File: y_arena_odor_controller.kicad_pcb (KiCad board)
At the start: 2 copper layers, 74.9 x 80.6 mm, 105 parts, among them P1 PWR_JACK_2.1x5.5_SMD_RA, SW1 SPDT_SLIDE_500A_SM, U1 DRV103, U2 DRV103, U3 DRV103, U4 DRV103, U5 DRV103, U6 DRV103, U7 DRV103, U8 DRV103, U9 DRV103

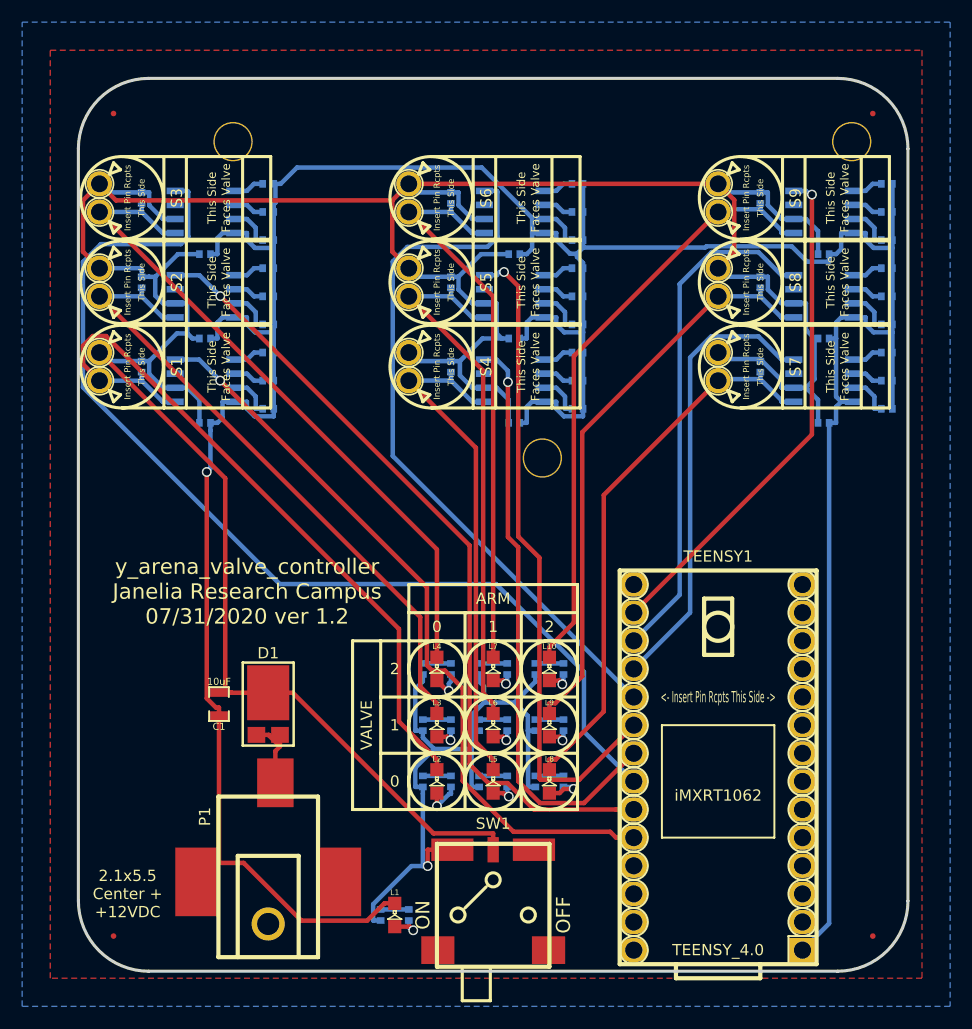
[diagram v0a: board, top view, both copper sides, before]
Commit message: valve -> odor
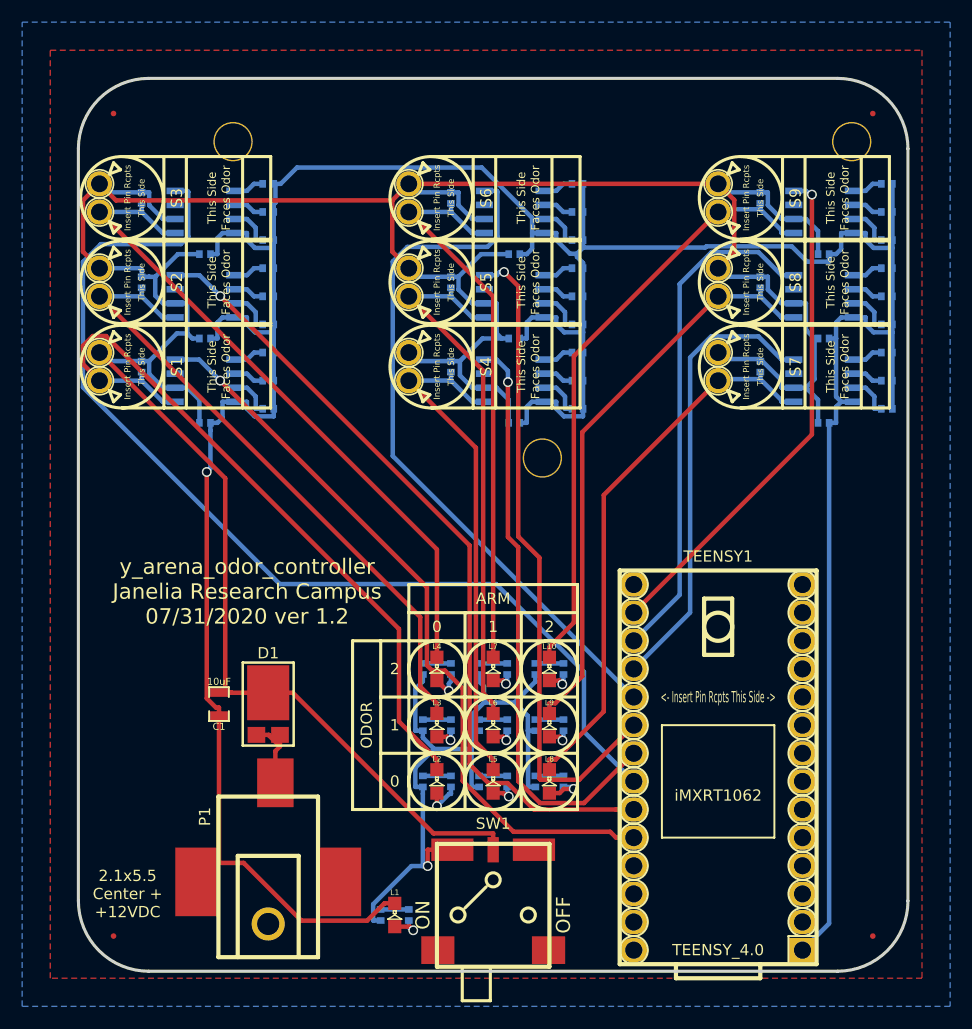
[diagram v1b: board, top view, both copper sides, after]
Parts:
- C1: footprint y_arena_valve_controller:SM0805 -> y_arena_odor_controller:SM0805
- C10, C12, C14, C16, C18, C2, C4, C6, C8, D10, D11, D12, D13, D14, D15, D16, D17, D18, D19, D20, D3, D4, D5, D6, D7, D8, D9: footprint valve_spike_hold:SM0402_POL -> odor_spike_hold:SM0402_POL
- C11, C13, C15, C17, C19, C3, C5, C7, C9, R10, R11, R12, R13, R14, R15, R16, R17, R18, R19, R2, R20, R21, R22, R23, R24, R25, R26, R27, R28, R3, R4, R5, R6, R7, R8, R9: footprint valve_spike_hold:SM0402 -> odor_spike_hold:SM0402
- D1: footprint y_arena_valve_controller:CFP15 -> y_arena_odor_controller:CFP15
- D2: footprint y_arena_valve_controller:SM0402_POL -> y_arena_odor_controller:SM0402_POL
- FID1, FID2, FID3, FID4: footprint y_arena_valve_controller:FIDUCIAL -> y_arena_odor_controller:FIDUCIAL
- L1: footprint y_arena_valve_controller:LED0805 -> y_arena_odor_controller:LED0805
- L10, L2, L3, L4, L5, L6, L7, L8, L9: footprint valve_spike_hold:LED0805 -> odor_spike_hold:LED0805
- MH1, MH2, MH3: footprint y_arena_valve_controller:MOUNTING_HOLE_4-40 -> y_arena_odor_controller:MOUNTING_HOLE_4-40
- P1: footprint y_arena_valve_controller:DCJACK_3PAD_SMD_RA -> y_arena_odor_controller:DCJACK_3PAD_SMD_RA
- R1: footprint y_arena_valve_controller:SM0402 -> y_arena_odor_controller:SM0402
- S1, S2, S3, S4, S5, S6, S7, S8, S9: footprint valve_spike_hold:LEECO_LHDB -> odor_spike_hold:LEECO_LHDB
- SW1: footprint y_arena_valve_controller:SPDT_SLIDE_500A_SM -> y_arena_odor_controller:SPDT_SLIDE_500A_SM
- TEENSY1: footprint y_arena_valve_controller:TEENSY_4.0 -> y_arena_odor_controller:TEENSY_4.0
- U1, U2, U3, U4, U5, U6, U7, U8, U9: footprint valve_spike_hold:SOIC_8 -> odor_spike_hold:SOIC_8
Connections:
- net /ARM_0_VALVE_0 renamed /ARM_0_ODOR_0
- net /ARM_0_VALVE_1 renamed /ARM_0_ODOR_1
- net /ARM_0_VALVE_2 renamed /ARM_0_ODOR_2
- net /ARM_1_VALVE_0 renamed /ARM_1_ODOR_0
- net /ARM_1_VALVE_1 renamed /ARM_1_ODOR_1
- net /ARM_1_VALVE_2 renamed /ARM_1_ODOR_2
- net /ARM_2_VALVE_0 renamed /ARM_2_ODOR_0
- net /ARM_2_VALVE_1 renamed /ARM_2_ODOR_1
- net /ARM_2_VALVE_2 renamed /ARM_2_ODOR_2
- net /valve_0/SH renamed /odor_0/SH
- net /valve_1/SH renamed /odor_1/SH
- net /valve_2/SH renamed /odor_2/SH
- net /valve_3/SH renamed /odor_3/SH
- net /valve_4/SH renamed /odor_4/SH
- net /valve_5/SH renamed /odor_5/SH
- net /valve_6/SH renamed /odor_6/SH
- net /valve_7/SH renamed /odor_7/SH
- net /valve_8/SH renamed /odor_8/SH
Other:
- board text added: "ODOR"
- board text added: "ODOR 0"
- board text added: "ODOR 1"
- board text added: "ODOR 2"
- board text added: "y_arena_odor_controller Janelia Research Campus 07/31/2020 ver 1.2"
- board text removed: "VALVE"
- board text removed: "VALVE 0"
- board text removed: "VALVE 1"
- board text removed: "VALVE 2"
- board text removed: "y_arena_valve_controller Janelia Research Campus 07/31/2020 ver 1.2"

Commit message: Switch arms from columns to rows and use odor instead of valve
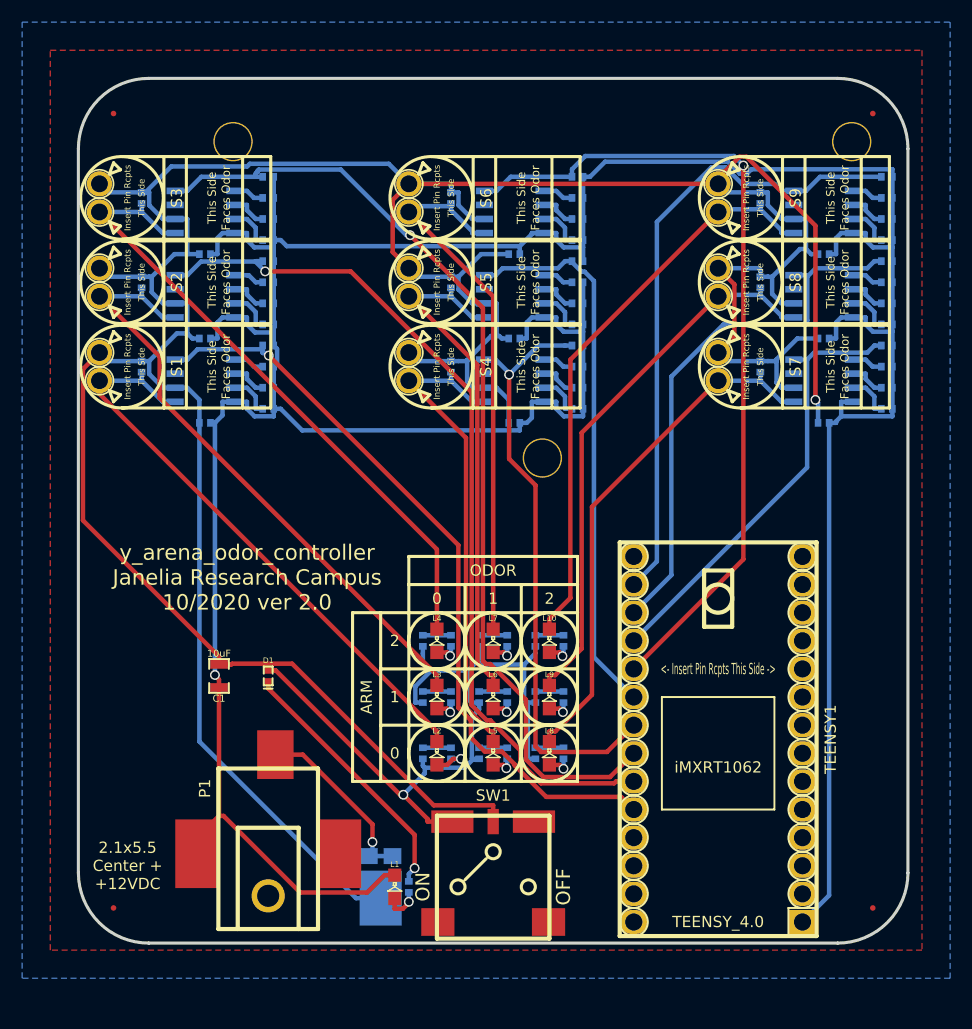
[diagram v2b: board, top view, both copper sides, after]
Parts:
- added R29: 205k, odor_spike_hold:SM0402, B.Cu at (123.8, 80.6)
- added R30: 390, odor_spike_hold:SM0402, B.Cu at (94.6, 106.7)
- added R31: 150k, odor_spike_hold:SM0402, B.Cu at (123.8, 67.3)
- added R32: 150k, odor_spike_hold:SM0402, B.Cu at (123.8, 69.2)
- added R33: 205k, odor_spike_hold:SM0402, B.Cu at (123.8, 73.0)
- added R34: 390, odor_spike_hold:SM0402, B.Cu at (94.6, 101.6)
- added R35: 150k, odor_spike_hold:SM0402, B.Cu at (123.8, 59.7)
- added R36: 150k, odor_spike_hold:SM0402, B.Cu at (123.8, 61.6)
- added R37: 205k, odor_spike_hold:SM0402, B.Cu at (123.8, 65.4)
- D1: value DIODE_SCHOTTKY_45V_10A -> DIODE_LOW_REV_CURRENT_0402; footprint y_arena_odor_controller:CFP15 -> y_arena_odor_controller:SM0402_POL
- D2: value DIODE_LOW_REV_CURRENT_0402 -> DIODE_SCHOTTKY_45V_10A; footprint y_arena_odor_controller:SM0402_POL -> y_arena_odor_controller:CFP15
- MH1, MH2, MH3: value VAL** -> MOUNTING_HOLE_4-40
- R10, R22: value 205k -> 390
- R11, R20, R23, R8: value 390 -> 150k
- R16, R19, R28, R4, R7: value 205k -> 150k
- R17, R5: value 390 -> 205k
- R18, R6: value 150k -> 390
- R21, R9: value 150k -> 205k
- S1, S2, S3, S4, S5, S6, S7, S8, S9: value VAL** -> LEECO_LHDB
- moved R11 58.7 mm to (67.9, 59.7), turned to 270 degrees
- moved R23 49.5 mm to (95.9, 59.7), turned to 270 degrees
- moved R18 46.8 mm to (89.5, 106.7), turned to 180 degrees
- moved R20 45.1 mm to (95.9, 69.2), turned to 270 degrees
- moved R6 42.1 mm to (84.5, 106.7), turned to 180 degrees
- moved R22 40.2 mm to (89.5, 101.6), turned to 180 degrees
- moved R10 39.8 mm to (84.5, 101.6), turned to 180 degrees
- moved R8 38.6 mm to (67.9, 69.2), turned to 270 degrees
- moved R5 33.0 mm to (67.9, 80.6), turned to 270 degrees
- moved R13 31.8 mm to (67.9, 65.4)
- moved R12 31.2 mm to (67.9, 61.6)
- moved R25 29.0 mm to (95.9, 65.4)
- moved R24 28.7 mm to (95.9, 61.6)
- moved R21 28.1 mm to (95.9, 73.0)
- moved R17 24.3 mm to (95.9, 80.6), turned to 270 degrees
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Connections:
- D1 pad 1: VCC -> Net-(D1-Pad1)
- D1 pad 2: VAA -> /Vled
- D2 pad 1: Net-(D2-Pad1) -> VCC
- D2 pad 2: /Vled -> VAA
- R1 pad 1: Net-(D2-Pad1) -> Net-(D1-Pad1)
- R10 pad 1: Net-(R10-Pad1) -> Net-(D7-Pad1)
- R10 pad 2: GND -> Net-(L4-Pad1)
- R11 pad 1: Net-(D9-Pad1) -> /ARM_2_ODOR_0
- R11 pad 2: Net-(L5-Pad1) -> GND
- R14 pad 1: Net-(D11-Pad1) -> Net-(D9-Pad1)
- R14 pad 2: Net-(L6-Pad1) -> Net-(L5-Pad1)
- R15 pad 1: Net-(R15-Pad1) -> /ARM_0_ODOR_1
- R17 pad 1: Net-(D13-Pad1) -> Net-(R17-Pad1)
- R17 pad 2: Net-(L7-Pad1) -> GND
- R18 pad 1: Net-(R18-Pad1) -> Net-(D11-Pad1)
- R18 pad 2: GND -> Net-(L6-Pad1)
- R19 pad 1: Net-(R19-Pad1) -> /ARM_1_ODOR_1
- R20 pad 1: Net-(D15-Pad1) -> Net-(R20-Pad1)
- R20 pad 2: Net-(L8-Pad1) -> GND
- R22 pad 1: Net-(R22-Pad1) -> Net-(D13-Pad1)
- R22 pad 2: GND -> Net-(L7-Pad1)
- R23 pad 1: Net-(D17-Pad1) -> /ARM_2_ODOR_1
- R23 pad 2: Net-(L9-Pad1) -> GND
- R26 pad 1: Net-(D19-Pad1) -> Net-(D15-Pad1)
- R26 pad 2: Net-(L10-Pad1) -> Net-(L8-Pad1)
- R27 pad 1: Net-(R27-Pad1) -> /ARM_0_ODOR_2
- R3 pad 1: Net-(R3-Pad1) -> /ARM_0_ODOR_0
- R5 pad 1: Net-(D5-Pad1) -> Net-(R5-Pad1)
- R5 pad 2: Net-(L3-Pad1) -> GND
- R6 pad 1: Net-(R6-Pad1) -> Net-(D5-Pad1)
- R6 pad 2: GND -> Net-(L3-Pad1)
- R7 pad 1: Net-(R7-Pad1) -> /ARM_1_ODOR_0
- R8 pad 1: Net-(D7-Pad1) -> Net-(R8-Pad1)
- R8 pad 2: Net-(L4-Pad1) -> GND
- TEENSY1 pad 15: /ARM_2_ODOR_1 -> /ARM_1_ODOR_2
- TEENSY1 pad 16: /ARM_2_ODOR_0 -> /ARM_0_ODOR_2
- TEENSY1 pad 17: /ARM_1_ODOR_2 -> /ARM_2_ODOR_1
- TEENSY1 pad 19: /ARM_1_ODOR_0 -> /ARM_0_ODOR_1
- TEENSY1 pad 20: /ARM_0_ODOR_2 -> /ARM_2_ODOR_0
- TEENSY1 pad 21: /ARM_0_ODOR_1 -> /ARM_1_ODOR_0
- U1 pad 1: Net-(R3-Pad1) -> Net-(R4-Pad1)
- U1 pad 3: Net-(R4-Pad1) -> Net-(R5-Pad1)
- U2 pad 1: Net-(R6-Pad1) -> Net-(R8-Pad1)
- U2 pad 3: Net-(R7-Pad1) -> Net-(R9-Pad1)
- U2 pad 8: /ARM_0_ODOR_1 -> /ARM_1_ODOR_0
- U3 pad 1: Net-(R9-Pad1) -> Net-(R12-Pad1)
- U3 pad 3: Net-(R10-Pad1) -> Net-(R13-Pad1)
- U3 pad 8: /ARM_0_ODOR_2 -> /ARM_2_ODOR_0
- U4 pad 1: Net-(R12-Pad1) -> Net-(R16-Pad1)
- U4 pad 3: Net-(R13-Pad1) -> Net-(R17-Pad1)
- U4 pad 8: /ARM_1_ODOR_0 -> /ARM_0_ODOR_1
- U5 pad 1: Net-(R15-Pad1) -> Net-(R20-Pad1)
- U5 pad 3: Net-(R16-Pad1) -> Net-(R21-Pad1)
- U6 pad 1: Net-(R18-Pad1) -> Net-(R24-Pad1)
- U6 pad 3: Net-(R19-Pad1) -> Net-(R25-Pad1)
- U6 pad 8: /ARM_1_ODOR_2 -> /ARM_2_ODOR_1
- U7 pad 1: Net-(R21-Pad1) -> Net-(R28-Pad1)
- U7 pad 3: Net-(R22-Pad1) -> Net-(R29-Pad1)
- U7 pad 8: /ARM_2_ODOR_0 -> /ARM_0_ODOR_2
- U8 pad 1: Net-(R24-Pad1) -> Net-(R32-Pad1)
- U8 pad 3: Net-(R25-Pad1) -> Net-(R33-Pad1)
- U8 pad 8: /ARM_2_ODOR_1 -> /ARM_1_ODOR_2
- U9 pad 1: Net-(R27-Pad1) -> Net-(R36-Pad1)
- U9 pad 3: Net-(R28-Pad1) -> Net-(R37-Pad1)
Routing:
- net VCC: track 286.7 -> 356.4 mm, vias 0 -> 1
- net /ARM_0_ODOR_2: track 94.7 -> 40.3 mm
- net /ARM_2_ODOR_0: track 41.3 -> 88.5 mm, vias 0 -> 1
- net /ARM_2_ODOR_1: track 46.3 -> 75.0 mm, vias 0 -> 1
- net /ARM_1_ODOR_0: track 53.1 -> 79.4 mm
- net Net-(D1-Pad1): track 0.00 -> 23.7 mm, vias 0 -> 1
- net /ARM_0_ODOR_1: track 73.0 -> 54.3 mm
- net GND: track 300.6 -> 318.6 mm
- net /ARM_1_ODOR_2: track 64.0 -> 49.6 mm
- net /odor_0/SH: track 66.2 -> 53.6 mm
- net /ARM_2_ODOR_2: track 46.2 -> 57.3 mm, vias 1 -> 0
- net VAA: track 7.09 -> 16.4 mm, vias 0 -> 1
- net /ARM_1_ODOR_1: track 59.6 -> 50.3 mm, vias 1 -> 0
- net /Vled: track 63.4 -> 69.9 mm
- net Net-(R19-Pad1): track 3.96 -> 0.00 mm
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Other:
- board size 74.9 x 80.6 mm -> 74.9 x 78.1 mm
- rule pad_to_mask_clearance: 0.05 -> 0
- board text added: "y_arena_odor_controller Janelia Research Campus 10/2020 ver 2.0"
- board text removed: "y_arena_odor_controller Janelia Research Campus 07/31/2020 ver 1.2"
